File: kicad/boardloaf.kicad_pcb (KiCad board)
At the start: 2 copper layers, 100 x 100 mm, 42 parts, among them J1 AudioJack4, J2 AudioJack4, SW1 SW_Push, SW10 SW_Push, SW11 SW_Push, SW12 SW_Push, SW13 SW_Push, SW14 SW_Push, SW15 SW_Push, SW16 SW_Push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

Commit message: get back to once you belong
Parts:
- removed JP3: SolderJumper_2_Open, Jumper:SolderJumper-2_P1.3mm_Open_TrianglePad1.0x1.5mm
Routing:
- net COL2: track 199.8 -> 93.0 mm, vias 2 -> 0
- net ROW4: track 82.2 -> 59.3 mm, vias 1 -> 0

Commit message: Update boardloaf.kicad_pcb
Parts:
- moved JP1 0.71 mm to (150.5, 124.5), turned to -90 degrees
- moved JP2 0.71 mm to (150.5, 124.5), turned to -90 degrees
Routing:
- net COL2: track 93.0 -> 114.6 mm
- net VCC: track 81.0 -> 79.5 mm
- net SERIAL: track 76.6 -> 75.1 mm
- net GND: vias 20 -> 19

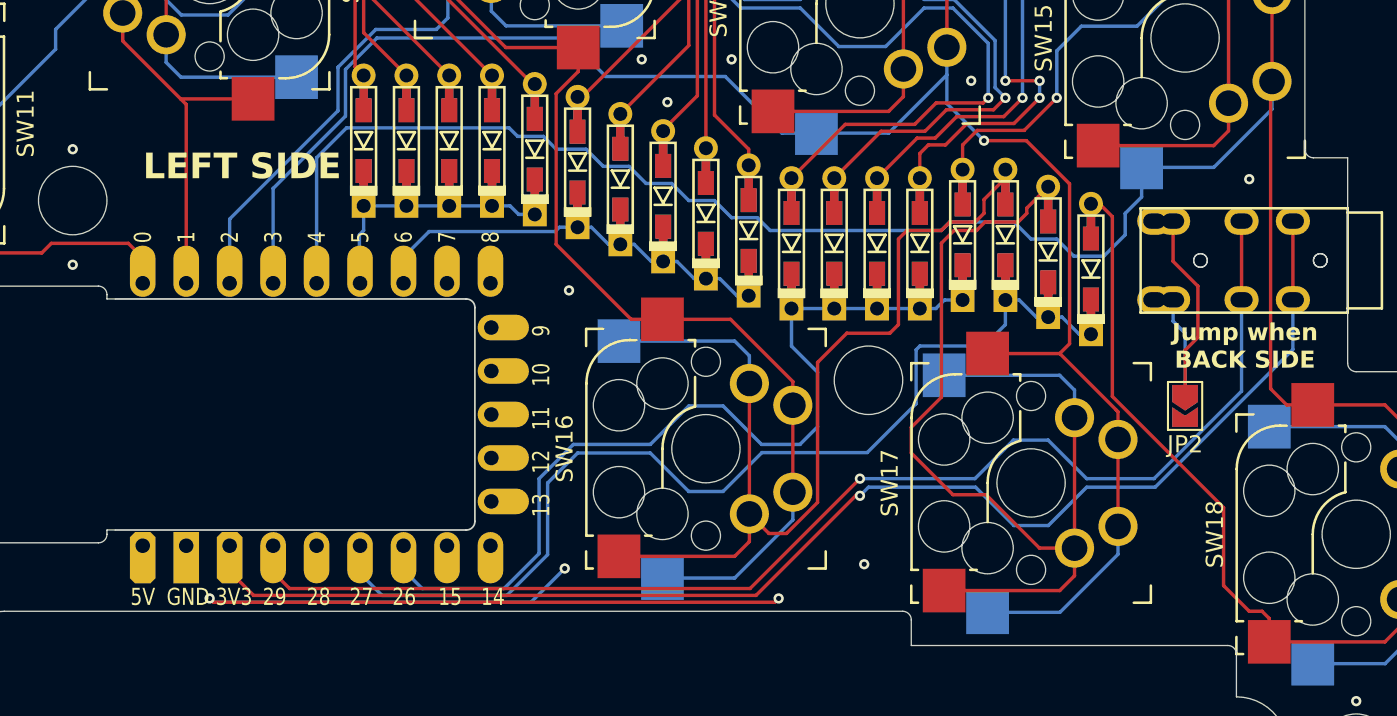
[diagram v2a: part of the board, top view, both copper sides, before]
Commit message: made jumper for reverse
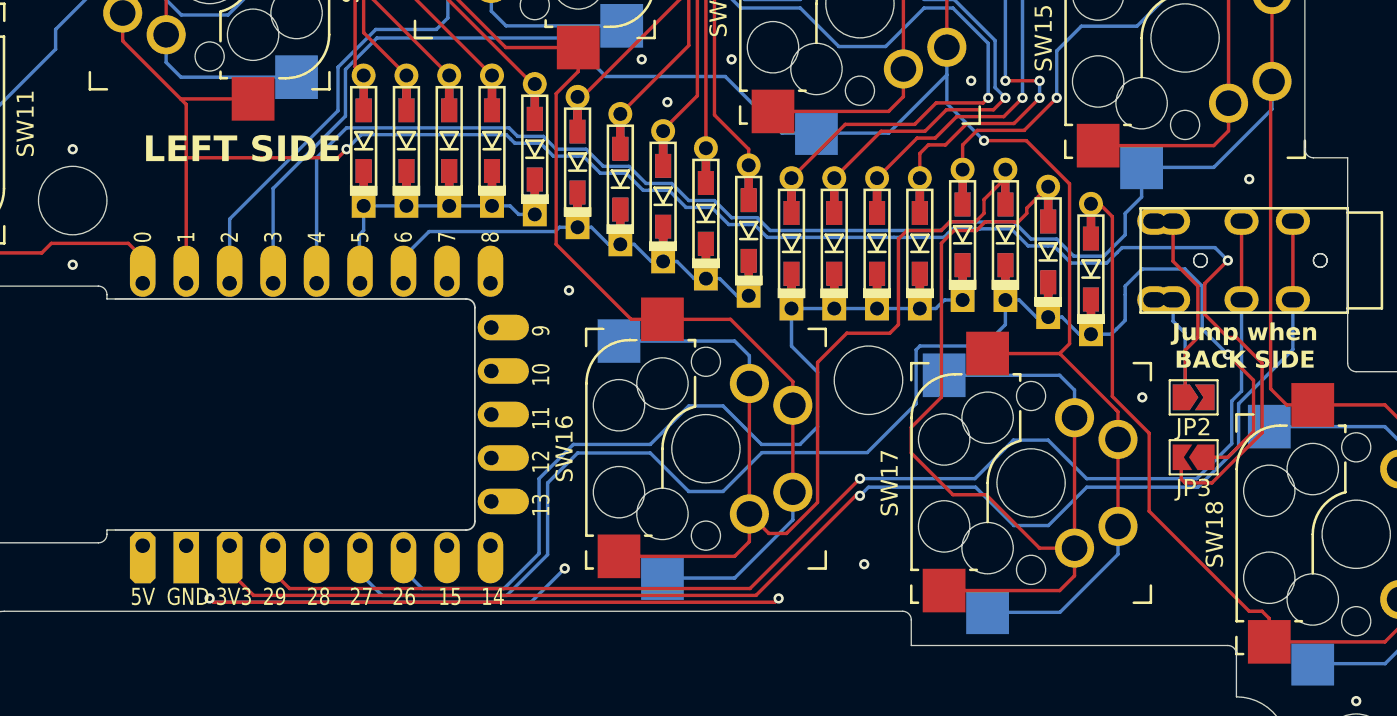
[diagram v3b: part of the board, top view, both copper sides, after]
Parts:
- added JP3: SolderJumper_2_Open, Jumper:SolderJumper-2_P1.3mm_Open_TrianglePad1.0x1.5mm, F.Cu at (151.0, 127.5)
- moved JP1 0.71 mm to (151.0, 124.0), turned to 0 degrees
- moved JP2 0.71 mm to (151.0, 124.0), turned to 0 degrees
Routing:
- net COL2: track 114.6 -> 199.8 mm, vias 0 -> 2
- net ROW4: track 59.3 -> 82.2 mm, vias 0 -> 1
- net VCC: track 79.5 -> 81.0 mm
- net SERIAL: track 75.1 -> 76.6 mm
- net GND: vias 19 -> 20
